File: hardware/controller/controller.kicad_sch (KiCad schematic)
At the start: 0 parts

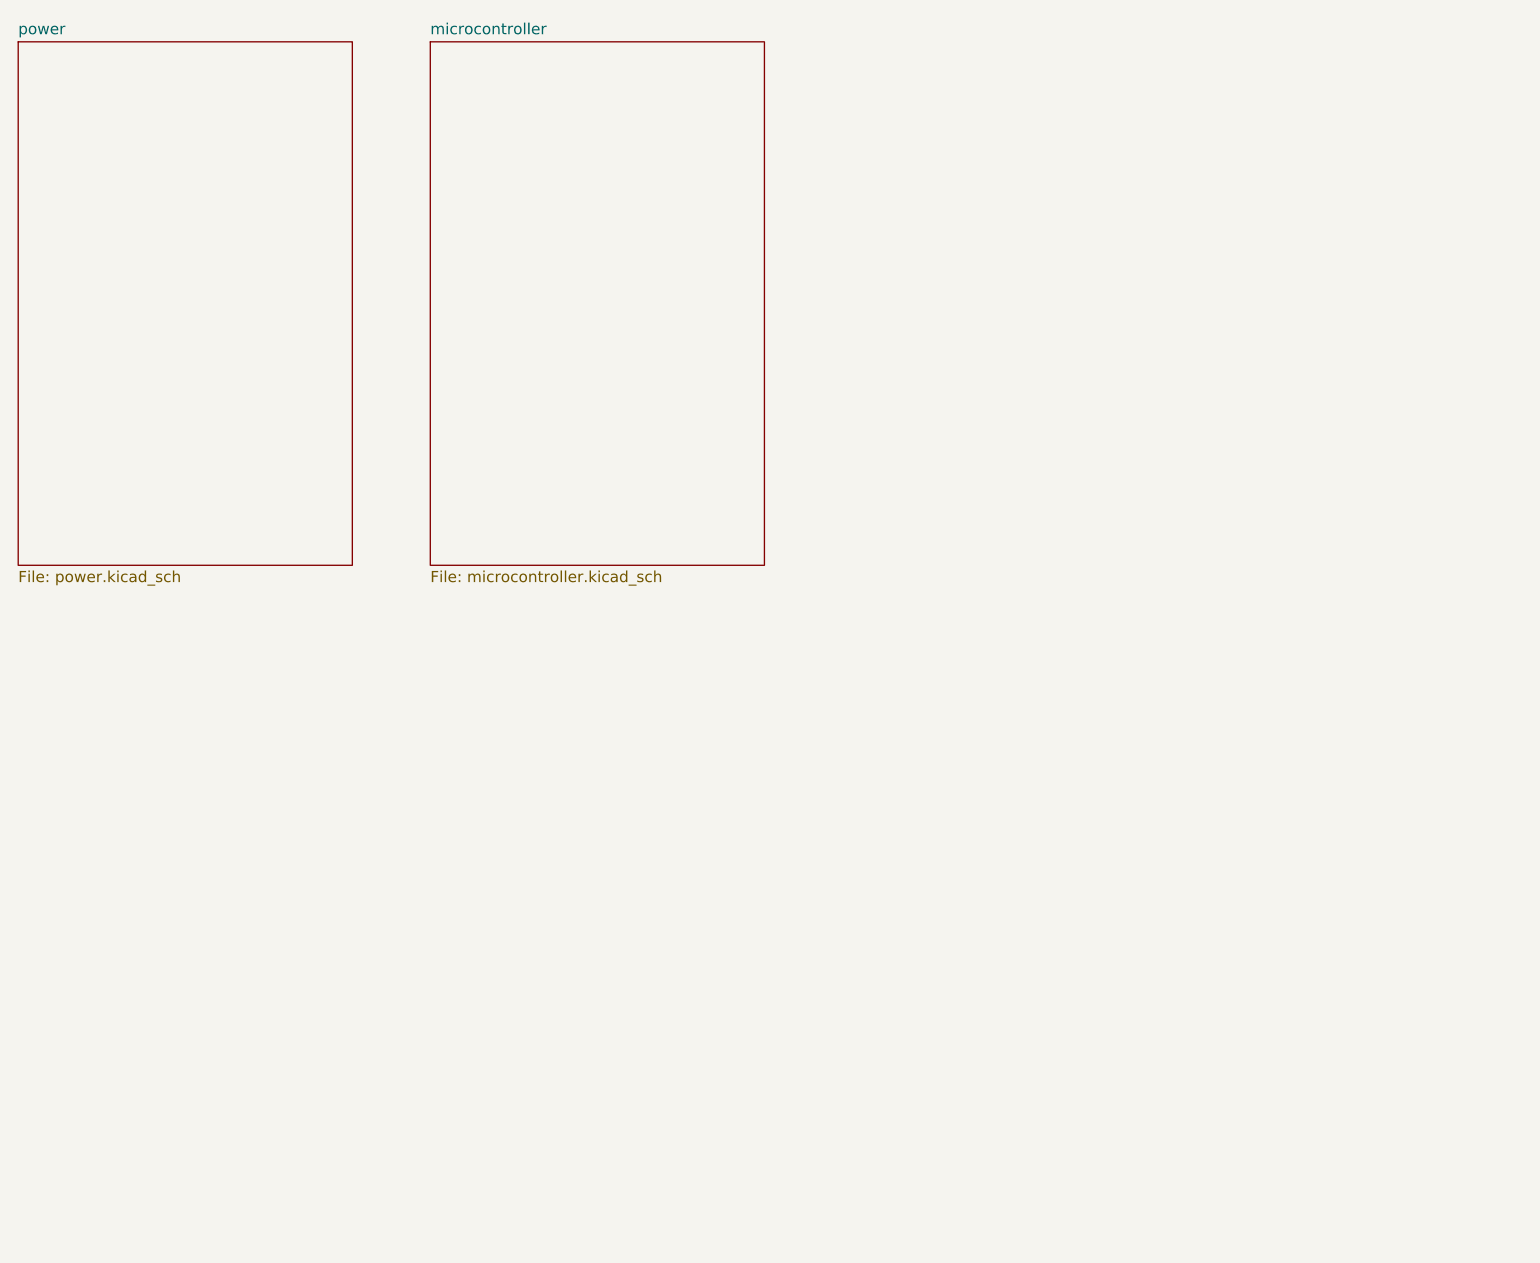
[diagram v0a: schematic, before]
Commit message: add IMU, FLOW, 5V, 3.3V, MOSFET SW
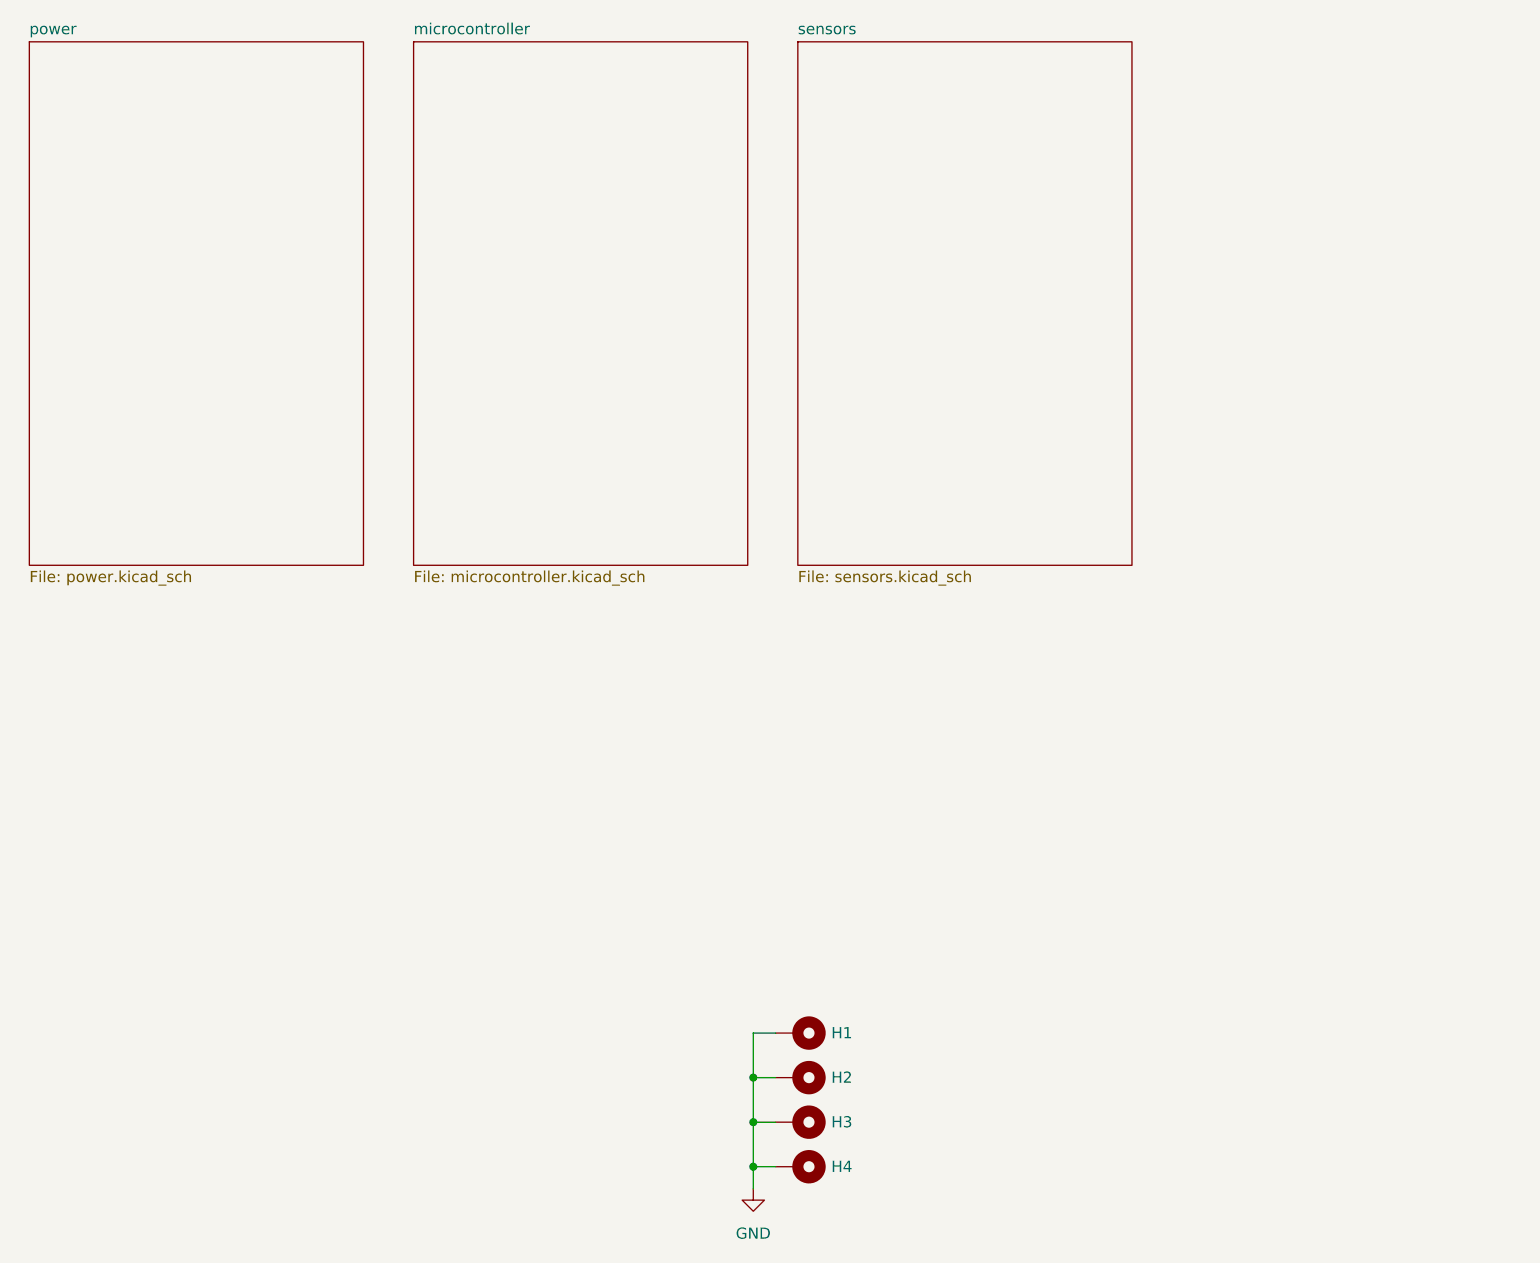
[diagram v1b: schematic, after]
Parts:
- added H1, H2, H3, H4: MountingHole_Pad, symbol Mechanical:MountingHole_Pad
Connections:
- new net GND: H1.1, H2.1, H3.1, H4.1
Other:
- added sheet sensors (sensors.kicad_sch)

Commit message: power stage development #1
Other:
- added sheet motor1 (motor1.kicad_sch)
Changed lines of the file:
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@@
+		)
+	)
+	(sheet
+		(at 195.58 50.8)
+		(size 38.1 59.69)
+		(fields_autoplaced yes)
+		(stroke
+			(width 0.1524)
+			(type solid)
+		)
+		(fill
+			(color 0 0 0 0.0000)
+		)
+		(property "Sheetname" "motor1"
+			(at 195.58 50.0884 0)
+			(effects
+				(font
+					(size 1.27 1.27)
+				)
+				(justify left bottom)
+			)
+		)
+		(property "Sheetfile" "motor1.kicad_sch"
+			(at 195.58 111.0746 0)
+			(effects
+				(font
+					(size 1.27 1.27)
+				)
+				(justify left top)
+			)
+		)
+		(instances
+			(project "controller"
+				(path "/b81e4285-7ba7-4843-ab37-49bb8c6c135f"
+					(page "6")
+				)
+			)
 		)
 	)

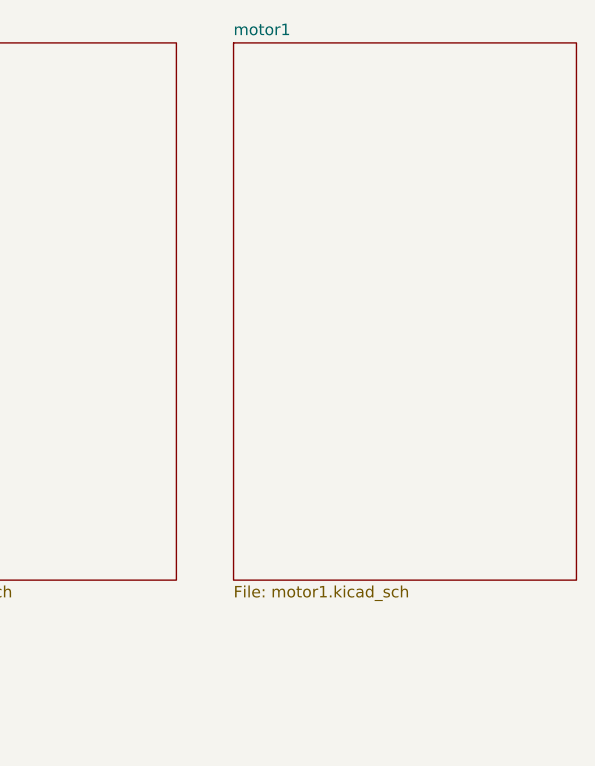
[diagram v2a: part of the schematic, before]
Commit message: uC pinout and second power stage
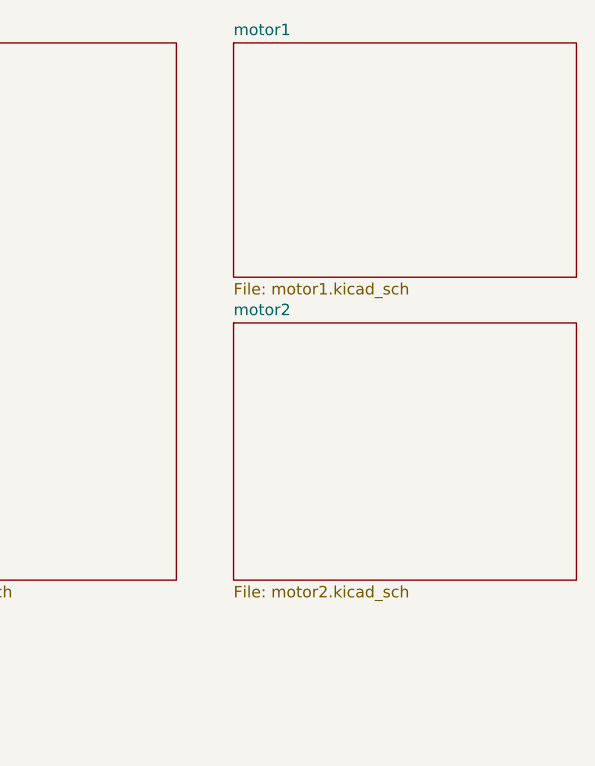
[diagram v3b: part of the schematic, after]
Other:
- added sheet motor2 (motor2.kicad_sch)
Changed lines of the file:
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@@
 	(title_block
 		(title "Hogger2 Controller")
-		(date "2024-10-28")
+		(date "2024-11-01")
 		(rev "V1.0")
 		(comment 4 "Author: Eryk Możdżeń")
@@
 	)
 	(sheet
+		(at 195.58 81.915)
+		(size 38.1 28.575)
+		(fields_autoplaced yes)
+		(stroke
+			(width 0.1524)
+			(type solid)
+		)
+		(fill
+			(color 0 0 0 0.0000)
+		)
+		(property "Sheetname" "motor2"
+			(at 195.58 81.2034 0)
+			(effects
+				(font
+					(size 1.27 1.27)
+				)
+				(justify left bottom)
+			)
+		)
+		(property "Sheetfile" "motor2.kicad_sch"
+			(at 195.58 111.0746 0)
+			(effects
+				(font
+					(size 1.27 1.27)
+				)
+				(justify left top)
+			)
+		)
+		(instances
+			(project "controller"
+				(path "/b81e4285-7ba7-4843-ab37-49bb8c6c135f"
+					(page "6")
+				)
+			)
+		)
+	)
+	(sheet
 		(at 151.13 50.8)
 		(size 38.1 59.69)
@@
 	(sheet
 		(at 195.58 50.8)
-		(size 38.1 59.69)
+		(size 38.1 26.035)
 		(fields_autoplaced yes)
 		(stroke
@@
 		)
 		(property "Sheetfile" "motor1.kicad_sch"
-			(at 195.58 111.0746 0)
-			(effects
-				(font
+			(at 195.58 77.4196 0)
+			(effects
+				(font

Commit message: change P-MOSFET on the battery enter
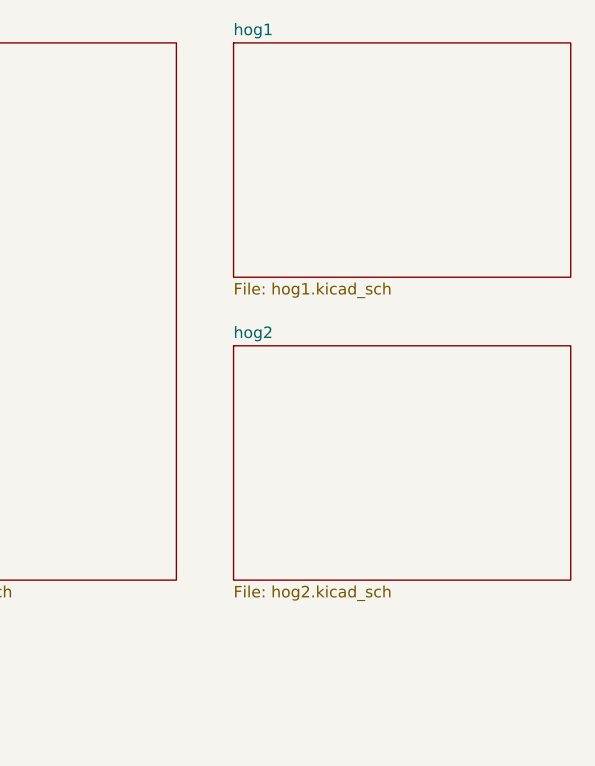
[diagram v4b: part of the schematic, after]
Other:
- removed sheet motor1
- removed sheet motor2
- added sheet hog1 (hog1.kicad_sch)
- added sheet hog2 (hog2.kicad_sch)
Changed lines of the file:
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@@
+	)
+	(sheet
+		(at 195.58 50.8)
+		(size 37.465 26.035)
+		(fields_autoplaced yes)
+		(stroke
+			(width 0.1524)
+			(type solid)
+		)
+		(fill
+			(color 0 0 0 0.0000)
+		)
+		(property "Sheetname" "hog1"
+			(at 195.58 50.0884 0)
+			(effects
+				(font
+					(size 1.27 1.27)
+				)
+				(justify left bottom)
+			)
+		)
+		(property "Sheetfile" "hog1.kicad_sch"
+			(at 195.58 77.4196 0)
+			(effects
+				(font
+					(size 1.27 1.27)
+				)
+				(justify left top)
+			)
+		)
+		(instances
+			(project "controller"
+				(path "/b81e4285-7ba7-4843-ab37-49bb8c6c135f"
+					(page "7")
+				)
+			)
+		)
 	)
 	(sheet
@@
 				(path "/b81e4285-7ba7-4843-ab37-49bb8c6c135f"
 					(page "3")
-				)
-			)
-		)
-	)
-	(sheet
-		(at 195.58 81.915)
-		(size 38.1 28.575)
-		(fields_autoplaced yes)
-		(stroke
-			(width 0.1524)
-			(type solid)
-		)
-		(fill
-			(color 0 0 0 0.0000)
-		)
-		(property "Sheetname" "motor2"
-			(at 195.58 81.2034 0)
-			(effects
-				(font
-					(size 1.27 1.27)
-				)
-				(justify left bottom)
-			)
-		)
-		(property "Sheetfile" "motor2.kicad_sch"
-			(at 195.58 111.0746 0)
-			(effects
-				(font
-					(size 1.27 1.27)
-				)
-				(justify left top)
-			)
-		)
-		(instances
-			(project "controller"
-				(path "/b81e4285-7ba7-4843-ab37-49bb8c6c135f"
-					(page "6")
 				)
 			)
@@
 	)
 	(sheet
-		(at 195.58 50.8)
-		(size 38.1 26.035)
+		(at 195.58 84.455)
+		(size 37.465 26.035)
 		(fields_autoplaced yes)
 		(stroke
@@
 			(color 0 0 0 0.0000)
 		)
-		(property "Sheetname" "motor1"
-			(at 195.58 50.0884 0)
+		(property "Sheetname" "hog2"
+			(at 195.58 83.7434 0)
 			(effects
 				(font
@@
 			)
 		)
-		(property "Sheetfile" "motor1.kicad_sch"
-			(at 195.58 77.4196 0)
+		(property "Sheetfile" "hog2.kicad_sch"
+			(at 195.58 111.0746 0)
 			(effects
 				(font
@@
 			(project "controller"
 				(path "/b81e4285-7ba7-4843-ab37-49bb8c6c135f"
-					(page "6")
+					(page "7")
 				)
 			)

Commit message: footprints, layout
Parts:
- H1, H2, H3, H4: footprint (none) -> MountingHole:MountingHole_3.2mm_M3_Pad_Via
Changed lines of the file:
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@@
 	(title_block
 		(title "Hogger2 Controller")
-		(date "2024-11-01")
+		(date "2024-11-03")
 		(rev "V1.0")
 		(comment 4 "Author: Eryk Możdżeń")
@@
 			)
 		)
-		(property "Footprint" ""
+		(property "Footprint" "MountingHole:MountingHole_3.2mm_M3_Pad_Via"
 			(at 151.13 163.83 0)
 			(effects
@@
 			)
 		)
-		(property "Footprint" ""
+		(property "Footprint" "MountingHole:MountingHole_3.2mm_M3_Pad_Via"
 			(at 151.13 179.07 0)
 			(effects
@@
 			)
 		)
-		(property "Footprint" ""
+		(property "Footprint" "MountingHole:MountingHole_3.2mm_M3_Pad_Via"
 			(at 151.13 168.91 0)
 			(effects
@@
 			)
 		)
-		(property "Footprint" ""
+		(property "Footprint" "MountingHole:MountingHole_3.2mm_M3_Pad_Via"
 			(at 151.13 173.99 0)
 			(effects
